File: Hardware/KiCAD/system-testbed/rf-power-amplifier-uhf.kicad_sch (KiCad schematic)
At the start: 22 parts, among them U1 GRF5604

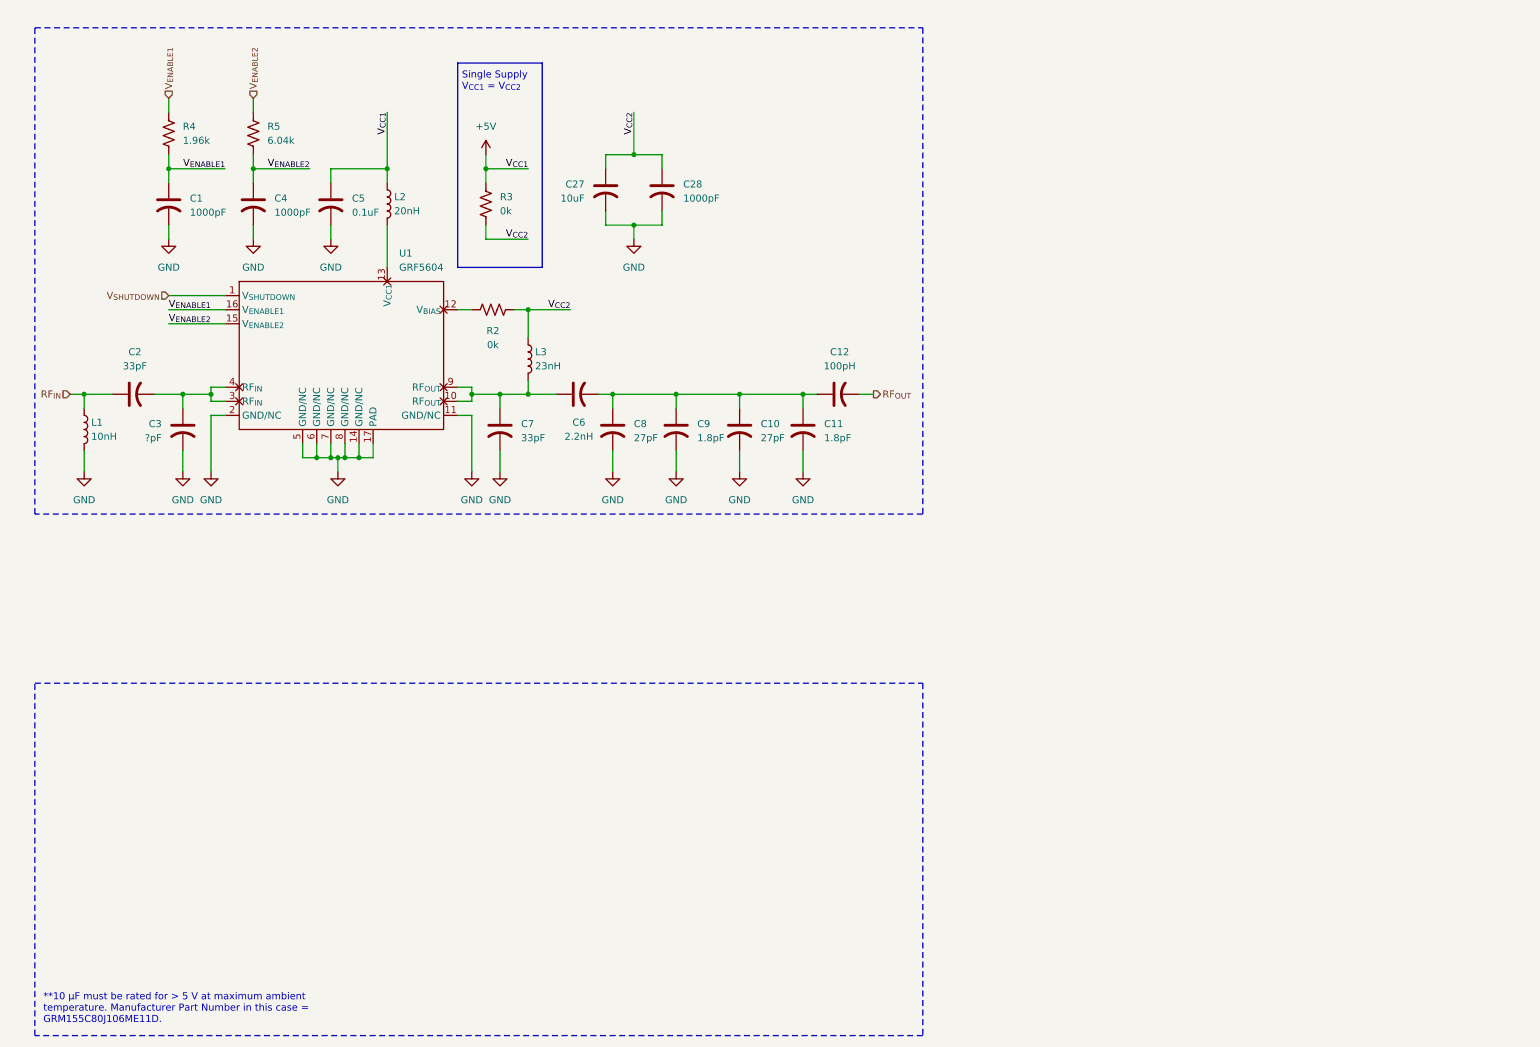
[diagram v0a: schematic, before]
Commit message: feat: begin dedicated sheets for RF switch throws, refine PA RFIC symbol #34
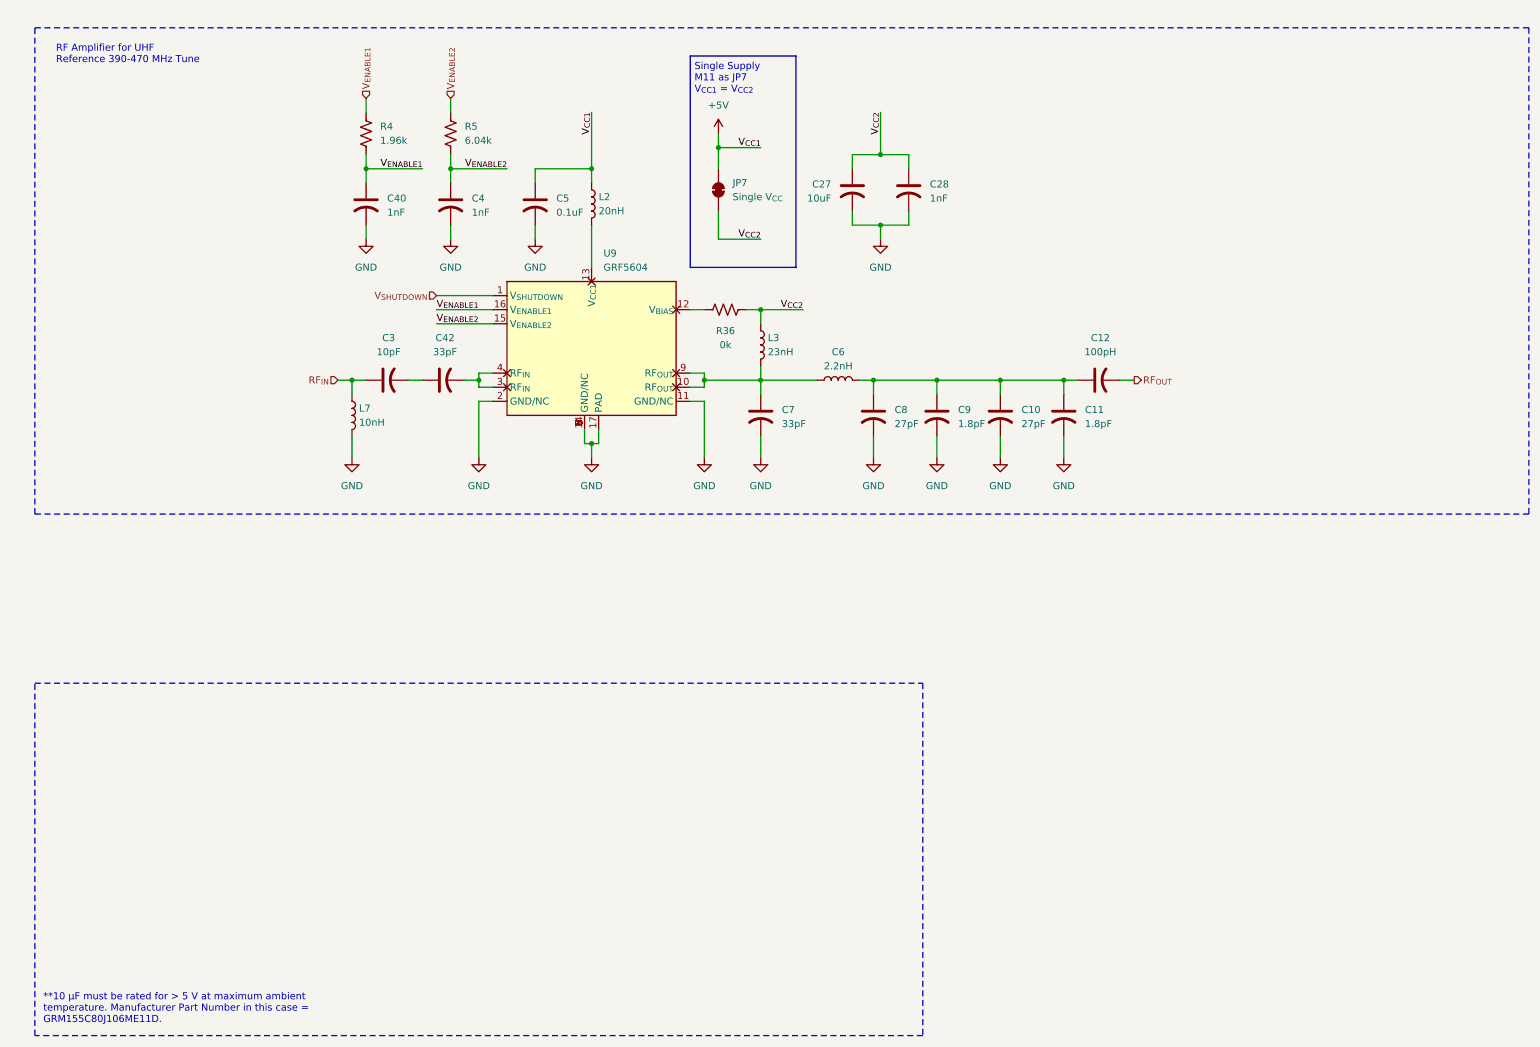
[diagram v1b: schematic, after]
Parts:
- removed R3: 0k, symbol Device:R_US
- added JP7: Single V_{CC}, Jumper:SolderJumper-2_P1.3mm_Open_RoundedPad1.0x1.5mm, symbol Jumper:SolderJumper_2_Bridged
- C28, C4: value 1000pF -> 1nF
- C3: value ?pF -> 10pF
- C40: renamed from C1; value 1000pF -> 1nF
- C6: symbol Device:C_US -> Device:L
- U9: renamed from U1; footprint (none) -> Package_DFN_QFN:QFN-16-1EP_3x3mm_P0.5mm_EP1.7x1.7mm_ThermalVias
- renumbered C2 to C42, L1 to L7, R2 to R36
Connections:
- net +5V: now also JP7.1 (A)
- net GND: no longer C3.2
- net RF_{IN}: now also C3.1; no longer C42.1
- net V_{CC2}: now also JP7.2 (B)
- net at C42.2, U9.3 (RF_{IN}), U9.4 (RF_{IN}): no longer C3.1
- new net: C3.2, C42.1
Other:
- note added: "RF Amplifier for UHF Reference 390-470 MHz Tune"
- note added: "Single Supply M11 as JP7 V_{CC1} = V_{CC2}"
- note removed: "Single Supply V_{CC1} = V_{CC2}"
- moved on the sheet: C10, C11, C12, C27, C28, C3, C4, C40, C42, C5, C7, C8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

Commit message: feat: refine rf subsystem sheet, specify band selection from two tuned PAs #34
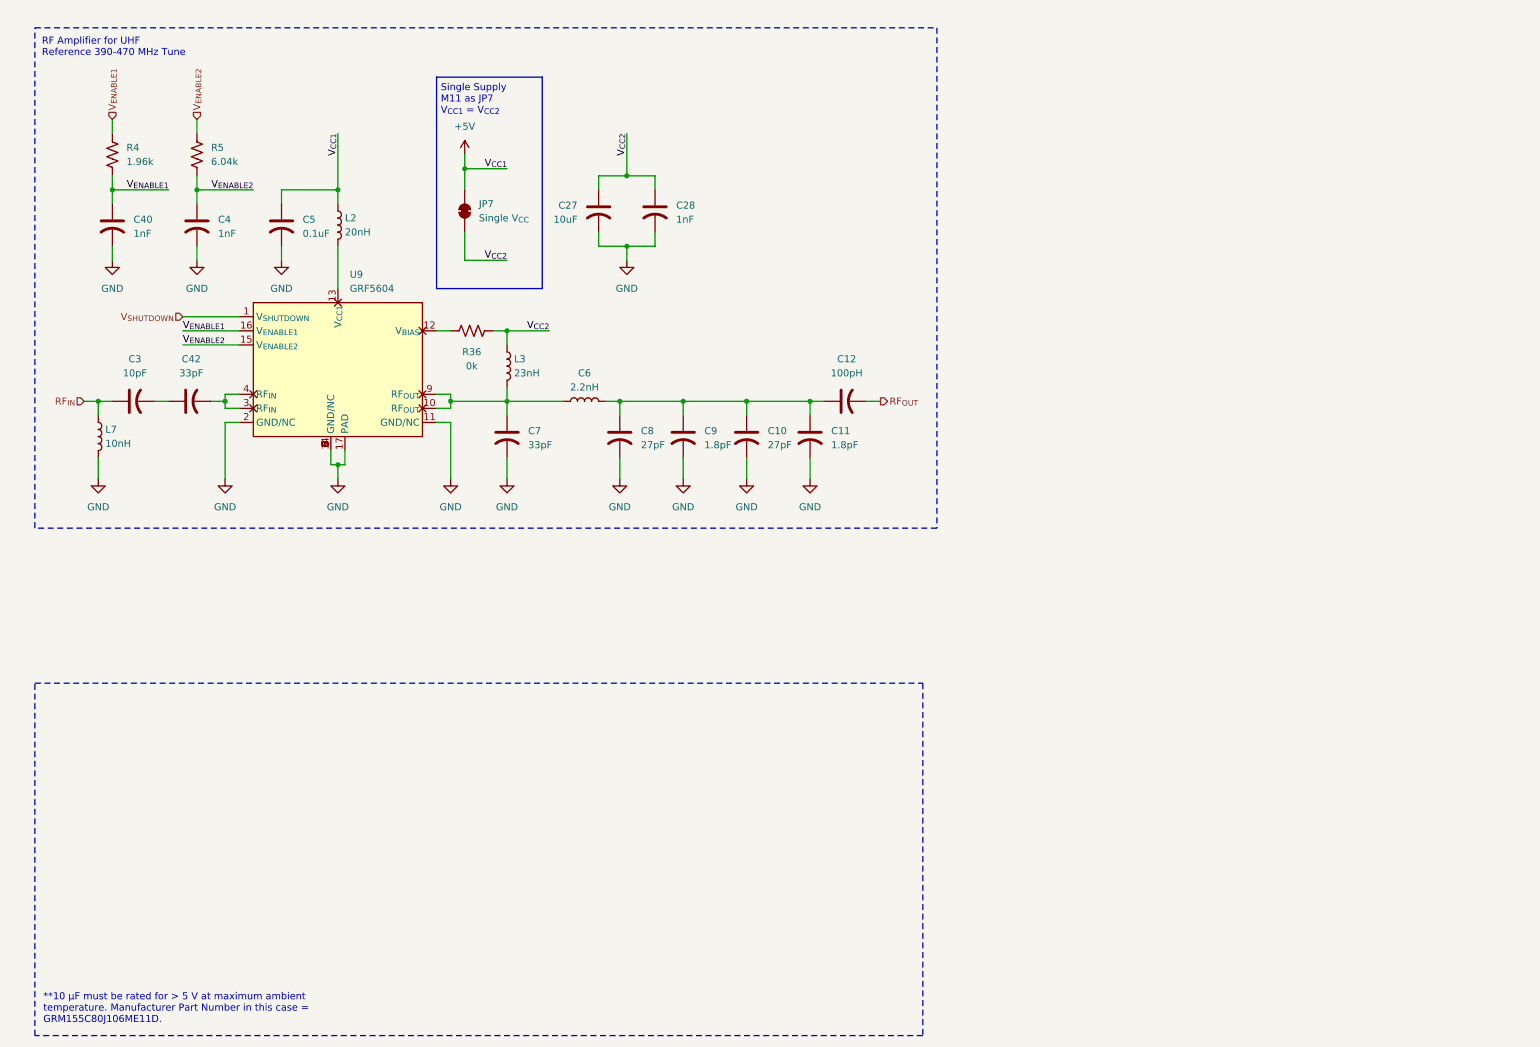
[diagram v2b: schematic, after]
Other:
- moved on the sheet: C10, C11, C12, C27, C28, C3, C4, C40, C42, C5, C6, C7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

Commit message: feat: complete RF switches, revise RF sheet structure #34
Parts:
- renumbered C40 to C23, C3 to C25, C42 to C26, C4 to C31, C5 to C32, C7 to C38, C6 to C39, C27 to C55, C8 to C56, C28 to C57, C9 to C58, C10 to C59, C11 to C60, C12 to C62, JP7 to JP9, L7 to L12, L2 to L13, L3 to L14, R36 to R14, R4 to R3, R5 to R6, U9 to U8
